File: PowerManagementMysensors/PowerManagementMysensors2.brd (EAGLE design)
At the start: 49.5 x 44.1 mm, 52 parts, among them IC2 AT25DF512C-SSHN-B, U1 LM8364BALMF20, U2 SI2399DS-T1-GE3, U3 SI2399DS-T1-GE3, U4 MCP1640BT-I/CHY, U5 TPS61222DCKT

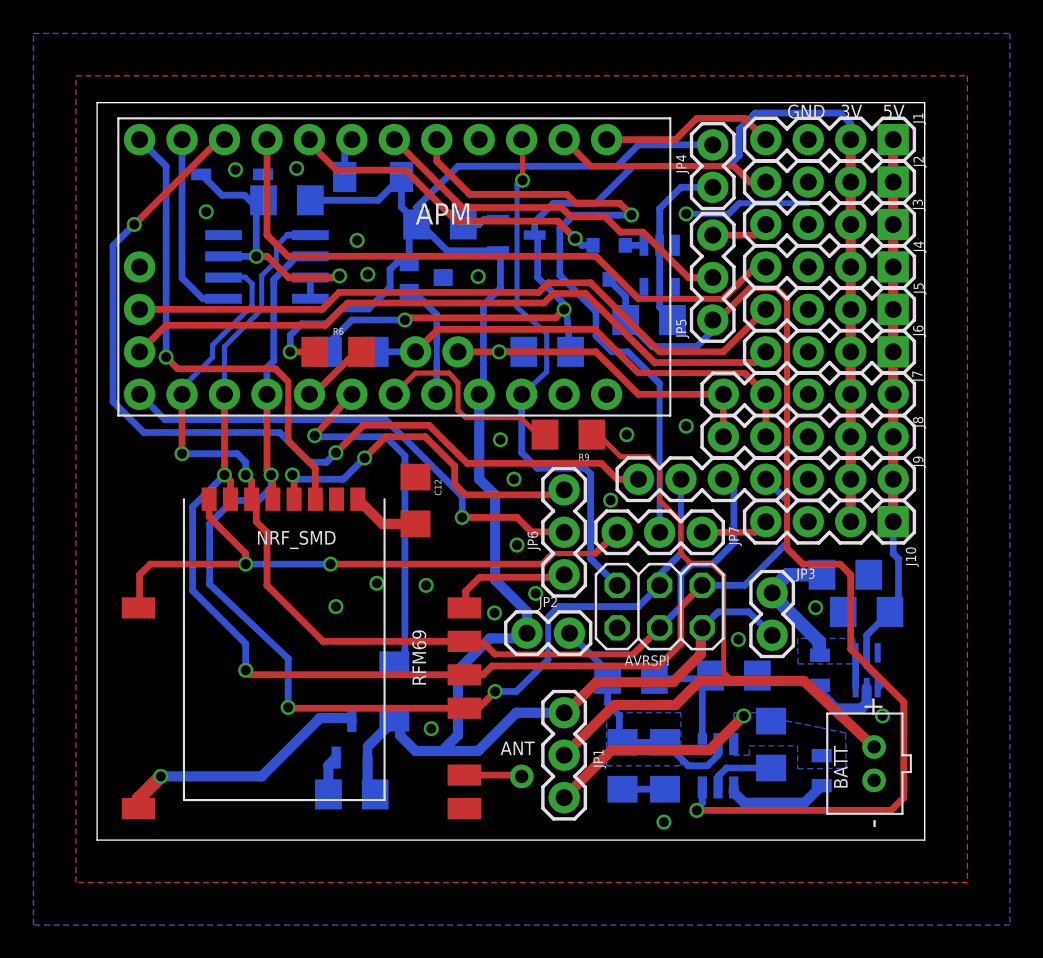
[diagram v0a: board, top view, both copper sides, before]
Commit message: gnd plane under nrf removed
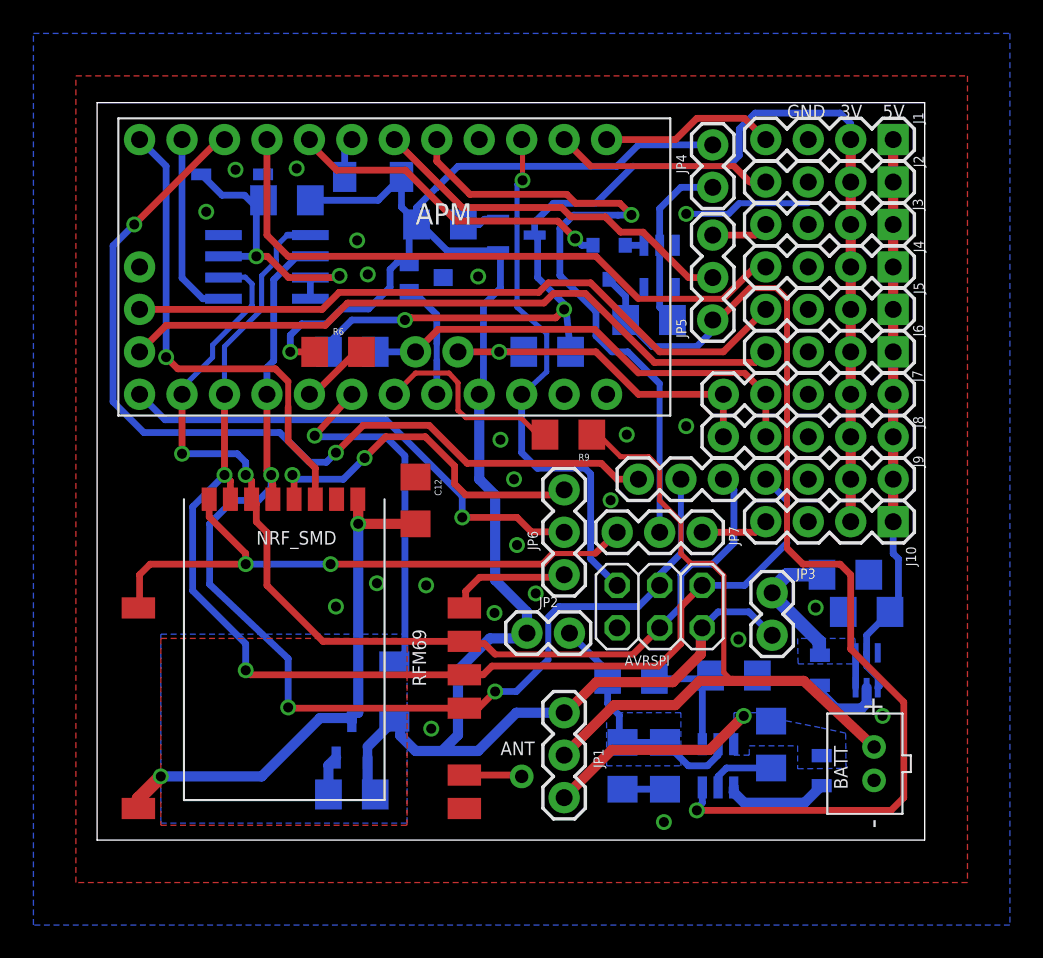
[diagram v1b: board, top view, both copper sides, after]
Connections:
- removed net N$15: C12.2, NRF_SMD.3V
- net VCC_RF: now also C12.2, NRF_SMD.3V
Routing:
- net VCC_RF: track 15.4 -> 32.5 mm, vias 1 -> 2
- net N$15: track 4.07 -> 0.00 mm
- added copper zone on layer 16, net N$15
- added copper zone on layer 1, net N$6
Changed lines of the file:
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@@
 <setting verticaltext="up"/>
 </settings>
-<grid distance="0.05" unitdist="inch" unit="mil" style="lines" multiple="1" display="yes" altdistance="1" altunitdist="mil" altunit="mil"/>
+<grid distance="0.05" unitdist="inch" unit="mil" style="lines" multiple="1" display="yes" altdistance="5" altunitdist="mil" altunit="mil"/>
 <layers>
 <layer number="1" name="Top" color="4" fill="1" visible="yes" active="yes"/>
@@
 </class>
 </classes>
-<designrules name="SeeedStudio_2layer_DRU_no_angle_20140221">
+<designrules name="LaenPCBOrder">
 <description language="de">&lt;b&gt;EAGLE Design Rules&lt;/b&gt;
 &lt;p&gt;
@@
 Einstellungen hier und speichern die Design Rules unter
 einem neuen Namen ab.</description>
-<description language="en">&lt;b&gt;EAGLE Design Rules&lt;/b&gt;
+<description language="en">&lt;b&gt;Laen's PCB Order Design Rules&lt;/b&gt;
 &lt;p&gt;
-The default Design Rules have been set to cover
-a wide range of applications. Your particular design
-may have different requirements, so please make the
-necessary adjustments and save your customized
-design rules under a new name.</description>
-<description language="zh">&lt;b&gt;Seeed Studio EAGLE Design Rules&lt;/b&gt;
-</description>
+Please make sure your boards conform to these design rules.</description>
 <param name="layerSetup" value="(1*16)"/>
-<param name="mtCopper" value="0.035mm 0.0175mm 0.035mm 0.035mm 0.035mm 0.035mm 0.035mm 0.035mm 0.035mm 0.035mm 0.035mm 0.035mm 0.035mm 0.035mm 0.0175mm 0.035mm"/>
-<param name="mtIsolate" value="1.5mm 1.1mm 0.2mm 0.15mm 0.2mm 0.15mm 0.2mm 0.15mm 0.2mm 0.15mm 0.2mm 0.15mm 0.2mm 0.15mm 0.2mm"/>
+<param name="mtCopper" value="0.0356mm 0.0356mm 0.0356mm 0.0356mm 0.0356mm 0.0356mm 0.0356mm 0.0356mm 0.0356mm 0.0356mm 0.0356mm 0.0356mm 0.0356mm 0.0356mm 0.0356mm 0.0356mm"/>
+<param name="mtIsolate" value="1.5011mm 0.1499mm 0.2007mm 0.1499mm 0.2007mm 0.1499mm 0.2007mm 0.1499mm 0.2007mm 0.1499mm 0.2007mm 0.1499mm 0.2007mm 0.1499mm 0.2007mm"/>
 <param name="mdWireWire" value="6mil"/>
 <param name="mdWirePad" value="6mil"/>
@@
 <param name="mdPadVia" value="6mil"/>
 <param name="mdViaVia" value="6mil"/>
-<param name="mdSmdPad" value="0mil"/>
-<param name="mdSmdVia" value="0mil"/>
-<param name="mdSmdSmd" value="0mil"/>
+<param name="mdSmdPad" value="6mil"/>
+<param name="mdSmdVia" value="6mil"/>
+<param name="mdSmdSmd" value="6mil"/>
 <param name="mdViaViaSameLayer" value="8mil"/>
 <param name="mnLayersViaInSmd" value="2"/>
-<param name="mdCopperDimension" value="10mil"/>
-<param name="mdDrill" value="10mil"/>
+<param name="mdCopperDimension" value="15mil"/>
+<param name="mdDrill" value="6mil"/>
 <param name="mdSmdStop" value="0mil"/>
 <param name="msWidth" value="6mil"/>
-<param name="msDrill" value="12mil"/>
-<param name="msMicroVia" value="12mil"/>
+<param name="msDrill" value="13mil"/>
+<param name="msMicroVia" value="13mil"/>
 <param name="msBlindViaRatio" value="0.5"/>
 <param name="rvPadTop" value="0.25"/>
@@
 <param name="rvMicroViaOuter" value="0.25"/>
 <param name="rvMicroViaInner" value="0.25"/>
-<param name="rlMinPadTop" value="10mil"/>
+<param name="rlMinPadTop" value="7mil"/>
 <param name="rlMaxPadTop" value="20mil"/>
-<param name="rlMinPadInner" value="10mil"/>
+<param name="rlMinPadInner" value="7mil"/>
 <param name="rlMaxPadInner" value="20mil"/>
-<param name="rlMinPadBottom" value="10mil"/>
+<param name="rlMinPadBottom" value="7mil"/>
 <param name="rlMaxPadBottom" value="20mil"/>
-<param name="rlMinViaOuter" value="6mil"/>
+<param name="rlMinViaOuter" value="7mil"/>
 <param name="rlMaxViaOuter" value="20mil"/>
-<param name="rlMinViaInner" value="6mil"/>
+<param name="rlMinViaInner" value="7mil"/>
 <param name="rlMaxViaInner" value="20mil"/>
 <param name="rlMinMicroViaOuter" value="4mil"/>
@@
 <param name="psTop" value="-1"/>
 <param name="psBottom" value="-1"/>
-<param name="psFirst" value="0"/>
+<param name="psFirst" value="-1"/>
 <param name="psElongationLong" value="100"/>
 <param name="psElongationOffset" value="100"/>
 <param name="mvStopFrame" value="1"/>
 <param name="mvCreamFrame" value="0"/>
-<param name="mlMinStopFrame" value="2mil"/>
-<param name="mlMaxStopFrame" value="2mil"/>
+<param name="mlMinStopFrame" value="3mil"/>
+<param name="mlMaxStopFrame" value="3mil"/>
 <param name="mlMinCreamFrame" value="0mil"/>
 <param name="mlMaxCreamFrame" value="0mil"/>
-<param name="mlViaStopLimit" value="100mil"/>
+<param name="mlViaStopLimit" value="0mil"/>
 <param name="srRoundness" value="0"/>
 <param name="srMinRoundness" value="0mil"/>
@@
 <param name="checkAngle" value="0"/>
 <param name="checkFont" value="1"/>
-<param name="checkRestrict" value="0"/>
+<param name="checkRestrict" value="1"/>
 <param name="useDiameter" value="13"/>
 <param name="maxErrors" value="50"/>
@@
 <wire x1="13.335" y1="7.3025" x2="15.0622" y2="7.3025" width="0.6096" layer="16"/>
 <wire x1="15.0622" y1="7.3025" x2="15.24" y2="7.1247" width="0.6096" layer="16"/>
+<contactref element="NRF_SMD" pad="3V"/>
+<contactref element="C12" pad="2"/>
+<wire x1="15.595" y1="20.395" x2="15.621" y2="20.395" width="0.4064" layer="1"/>
+<wire x1="15.24" y1="7.62" x2="15.24" y2="7.1247" width="0.6096" layer="16"/>
+<wire x1="15.621" y1="7.62" x2="15.24" y2="7.62" width="0.6096" layer="16"/>
+<wire x1="15.621" y1="20.395" x2="15.621" y2="18.923" width="0.6096" layer="1"/>
+<via x="15.621" y="18.923" extent="1-16" drill="0.6" shape="square"/>
+<wire x1="19.05" y1="18.92" x2="15.621" y2="18.92" width="0.6096" layer="1"/>
+<wire x1="15.621" y1="18.92" x2="15.621" y2="18.923" width="0.6096" layer="1"/>
+<wire x1="15.621" y1="7.62" x2="15.621" y2="18.923" width="0.6096" layer="16"/>
 </signal>
 <signal name="SCK">
@@
 <wire x1="19.05" y1="27.94" x2="17.78" y2="26.67" width="0.3048" layer="1"/>
 </signal>
-<signal name="N$15">
-<contactref element="NRF_SMD" pad="3V"/>
-<contactref element="C12" pad="2"/>
-<wire x1="19.05" y1="18.92" x2="17.07" y2="18.92" width="0.6096" layer="1"/>
-<wire x1="17.07" y1="18.92" x2="15.595" y2="20.395" width="0.6096" layer="1"/>
-</signal>
 <signal name="N$16">
 <contactref element="IC2" pad="7"/>
@@
 <wire x1="29.0068" y1="35.5854" x2="28.6004" y2="35.9918" width="0.4064" layer="16"/>
 </signal>
+<signal name="N$6">
+<polygon width="0" layer="1" pour="cutout">
+<vertex x="3.81" y="0.889"/>
+<vertex x="18.542" y="0.889"/>
+<vertex x="18.542" y="12.065"/>
+<vertex x="3.81" y="12.065"/>
+</polygon>
+</signal>
+<signal name="N$15">
+<polygon width="0" layer="16" pour="cutout">
+<vertex x="3.81" y="12.319"/>
+<vertex x="3.81" y="1.016"/>
+<vertex x="18.542" y="1.016"/>
+<vertex x="18.542" y="12.319"/>
+</polygon>
+</signal>
 </signals>

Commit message: gnd plane modified for nrf24
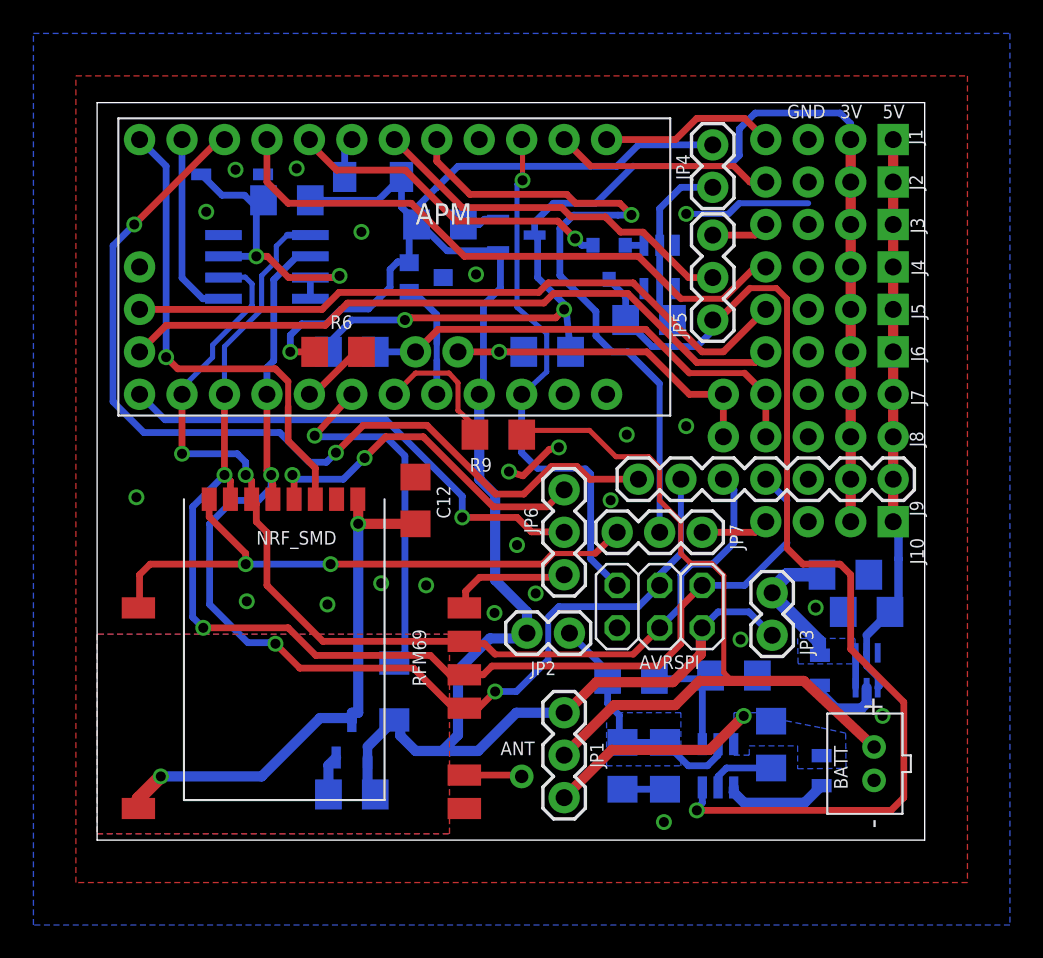
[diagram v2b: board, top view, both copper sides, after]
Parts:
- J1, J10, J2, J3, J4, J5, J6: device SparkFun-Connectors:1X04 -> SparkFun-Connectors:1X04_NO_SILK
- J7, J8: device SparkFun-Connectors:1X05 -> SparkFun-Connectors:1X05_NO_SILK
- moved R9 4.19 mm to (24.0, 24.3)
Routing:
- net VIN: track 42.7 -> 47.1 mm
- net N$14: track 12.0 -> 8.35 mm
- net GND: track 14.2 -> 17.8 mm
- net PWM: track 37.9 -> 36.1 mm
- net SPI_CSN: track 53.8 -> 55.2 mm
- net SCK: track 68.2 -> 67.3 mm

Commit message: Mosfet + Pull up on LM8364 reset
Pull up on lm8364 was missing. oops. So mosfet and pull up added to
invert signal. Schem changed. Little change for radios gnd plane. BOM
changed
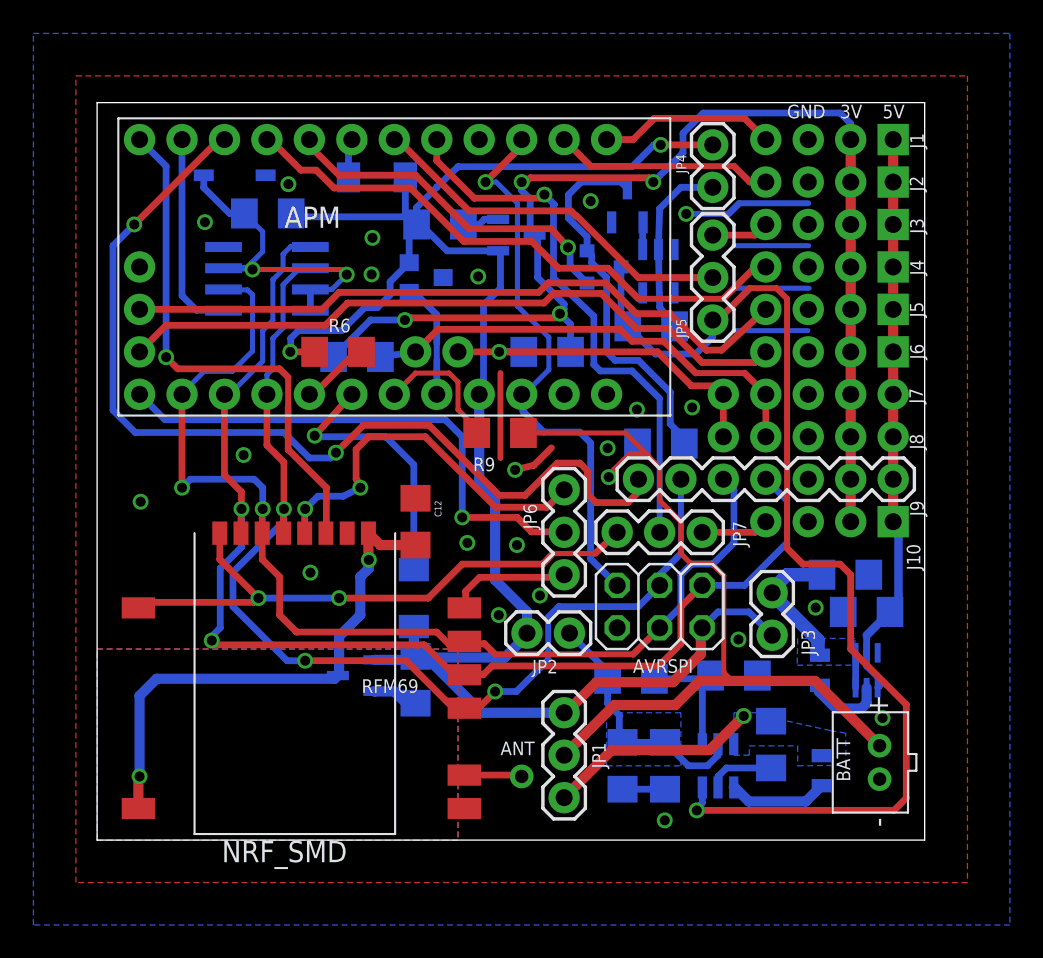
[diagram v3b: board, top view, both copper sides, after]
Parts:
- added R11: 10k, SparkFun-Passives:1206
- added U6: BSS123-7-F, pmo_lib:SOT95P240X110-3N
- D2: value BZT52H-B3V6 -> LL103A-GS08TR-ND; device adafruit:SOD-123 -> semicon-smd-ipc:SOD80
- D3: value LL103A-GS08TR-ND -> BZT52H-B3V6; device semicon-smd-ipc:SOD80 -> adafruit:SOD-123
- moved D3 32.3 mm to (8.23, 39.8), turned to 180 degrees
- moved D2 27.6 mm to (18.9, 14.5), turned to 270 degrees
- moved R5 7.85 mm to (19.1, 9.59), turned to 270 degrees
- moved U3 3.82 mm to (15.5, 9.84), turned to 0 degrees
- moved NRF_SMD 2.13 mm to (11.4, 8.76)
- moved R10 1.39 mm to (10.2, 37.5)
- moved C12 1.27 mm to (19.1, 19.1)
- moved IC2 0.71 mm to (10.2, 33.6)
- moved R8 0.43 mm to (15.5, 28.9)
- moved D6 0.42 mm to (30.3, 34.3), turned to 270 degrees
- moved R4 0.40 mm to (33.1, 30.7)
- moved BATT 0.34 mm to (46.8, 4.65)
- moved U1 0.27 mm to (33.6, 34.0)
- moved D1 0.23 mm to (16.7, 39.6)
- moved R9 0.14 mm to (24.1, 24.4)
- renumbered U$5 to ANT
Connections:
- removed net N$16: D2.C, IC2.3, IC2.7, IC2.8, R10.1
- new net N$17: D6.2, R11.1, U6.3
- new net N$6: D3.C, IC2.3, IC2.7, IC2.8, R10.1
- net EN_POWERRF: now also D2.1; no longer D3.1
- net GND: now also D3.A, U6.2; no longer D2.A
- net N$5: now also U6.1; no longer D6.2
- net VCC: now also D2.2; no longer D3.2
- net VIN: now also R11.2
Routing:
- net N$17: track 0.00 -> 22.6 mm
- net N$6: track 0.00 -> 19.2 mm, vias 0 -> 2
- net N$16: track 18.2 -> 0.00 mm, vias 2 -> 0
- net GND: track 17.8 -> 35.3 mm, vias 23 -> 22
- net D2: track 40.1 -> 33.0 mm
- net VIN: track 47.1 -> 53.1 mm, vias 0 -> 1
- net EN_POWERRF: track 21.9 -> 16.3 mm
- net VCC: track 118.7 -> 113.7 mm, vias 1 -> 2
- net SCK: track 67.3 -> 64.3 mm
- net SPI_CSN: track 55.2 -> 58.0 mm
- net D9: track 29.3 -> 31.8 mm
- net MOSI: track 63.5 -> 66.0 mm
- net VCC_SENSORS: track 70.6 -> 72.8 mm, vias 2 -> 4
- net D10: track 29.6 -> 31.6 mm
- net RF24_CSN: track 21.1 -> 22.7 mm
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- added copper zone on layer 1, net N$15
- added copper zone on layer 16, net N$16
- removed copper zone on layer 16, net N$15
- removed copper zone on layer 1, net N$6

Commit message: change on mosfet power (error in previous version)
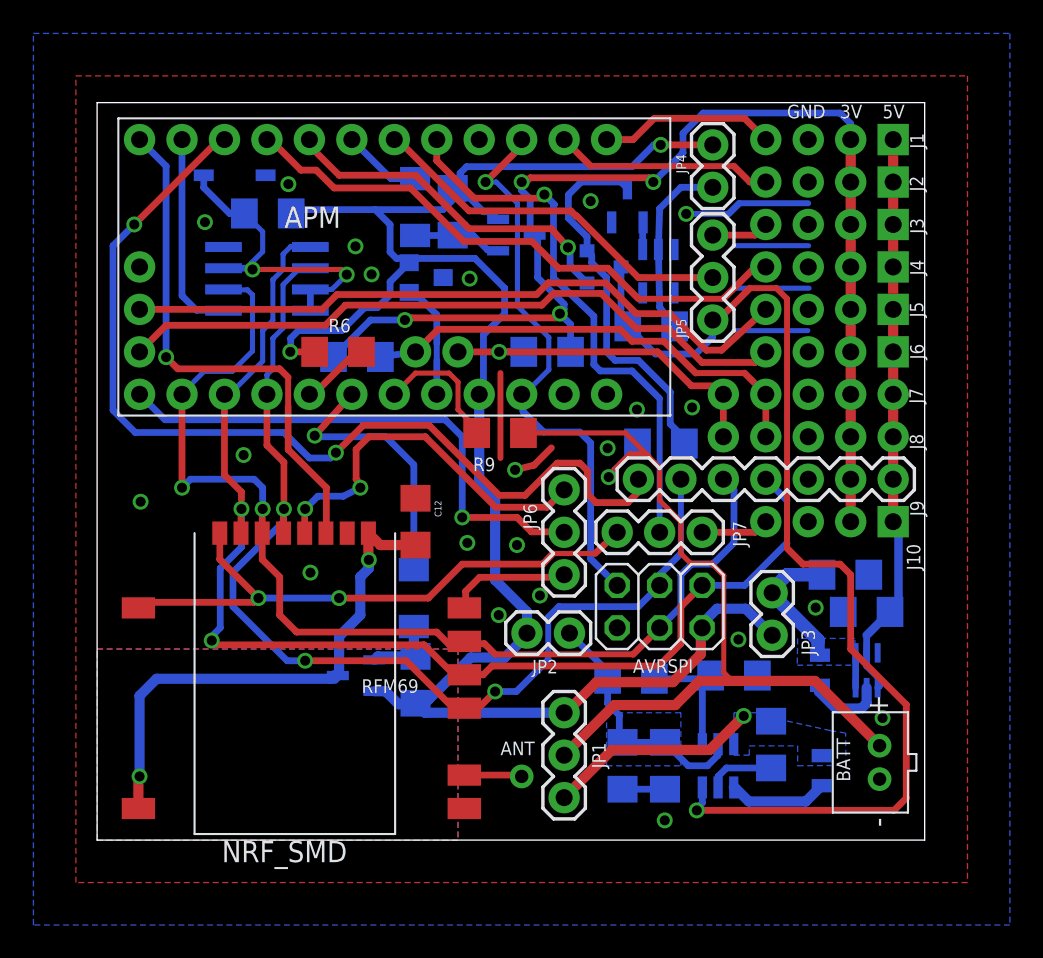
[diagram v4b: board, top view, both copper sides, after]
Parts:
- moved D1 2.90 mm to (19.0, 37.9), turned to 270 degrees
- moved R3 1.08 mm to (21.3, 37.6), turned to 90 degrees
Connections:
- removed net N$3: R3.2, U2.2
- new net N$18: D2.2, R5.1, U3.1
- net N$7: now also D1.2, R3.1, U2.1; no longer R5.2, U3.2
- net VCC: now also R3.2, R5.2, U2.2, U3.2; no longer D1.2, D2.2, R3.1, R5.1, U2.1, U3.1
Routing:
- net N$18: track 0.00 -> 4.38 mm
- net EN_POWER: track 2.43 -> 5.13 mm
- net N$7: track 2.76 -> 5.36 mm
- net N$3: track 2.22 -> 0.00 mm
- net VCC: track 113.7 -> 114.5 mm
